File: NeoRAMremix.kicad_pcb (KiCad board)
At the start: 2 copper layers, 58.4 x 88.4 mm, 26 parts, among them P1 C64-Exp-Port, Q1 2N3904, U1 HM628512BFP-5, U2 HM628512BFP-5, U3 HM628512BFP-5, U4 HM628512BFP-5

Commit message: More layout.
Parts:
- moved SJ1 167.2 mm to (90.2, 73.5)
- moved SJ2 153.9 mm to (92.7, 73.5)
- moved SJ3 152.5 mm to (96.5, 73.5)
- moved SJ4 149.4 mm to (99.1, 73.5)
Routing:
- net GND: track 443.4 -> 537.4 mm, vias 7 -> 10
- net +BATT: track 0.00 -> 63.3 mm
- net +5V: track 56.8 -> 80.1 mm, vias 1 -> 4
- net Net-(BT1-Pad1): track 0.00 -> 11.6 mm
- net Net-(SJ3-Pad1): track 0.00 -> 11.2 mm, vias 0 -> 1
- net Net-(SJ4-Pad1): track 0.00 -> 7.01 mm
- net /A7: track 13.3 -> 14.6 mm
- net /A6: track 12.5 -> 13.7 mm

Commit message: More layout.
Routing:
- net /RA15: track 0.00 -> 88.8 mm, vias 0 -> 1
- net Net-(U4-Pad24): track 0.00 -> 85.9 mm, vias 0 -> 1
- net /RA13: track 0.00 -> 79.7 mm, vias 0 -> 1
- net Net-(U4-Pad29): track 0.00 -> 79.7 mm, vias 0 -> 1
- net /RA17: track 0.00 -> 78.1 mm, vias 0 -> 1
- net /RA18: track 0.00 -> 74.8 mm, vias 0 -> 1
- net /RA8: track 0.00 -> 73.6 mm, vias 0 -> 1
- net /RA9: track 0.00 -> 72.4 mm, vias 0 -> 1
- net /RA16: track 0.00 -> 68.3 mm, vias 0 -> 1
- net /RA12: track 0.00 -> 66.7 mm, vias 0 -> 1
- net /RA11: track 0.00 -> 65.2 mm, vias 0 -> 1
- net /RA14: track 0.00 -> 64.7 mm, vias 0 -> 1
- net Net-(U3-Pad24): track 0.00 -> 59.3 mm, vias 0 -> 1
- net /D3: track 69.9 -> 126.7 mm, vias 0 -> 1
- net /D4: track 71.5 -> 123.8 mm, vias 0 -> 2
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
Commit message: First complete layout.
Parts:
- added G***: LOGO, Logo:bigby2, F.Cu at (113.2, 59.3)
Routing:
- net /A6: track 61.0 -> 132.0 mm, vias 1 -> 4
- net /A7: track 61.9 -> 120.7 mm, vias 1 -> 3
- net Net-(V1-Pad7): track 0.00 -> 45.5 mm
- net /A0: track 60.6 -> 102.2 mm, vias 1 -> 2
- net Net-(Q1-Pad3): track 51.3 -> 91.7 mm, vias 0 -> 1
- net Net-(SJ3-Pad1): track 11.2 -> 50.4 mm
- net Net-(SJ4-Pad1): track 7.01 -> 42.6 mm
- net Net-(V1-Pad9): track 0.00 -> 25.1 mm
- net /RA15: track 88.8 -> 68.6 mm
- net GND: track 566.7 -> 577.9 mm
- net /D3: track 126.7 -> 128.9 mm

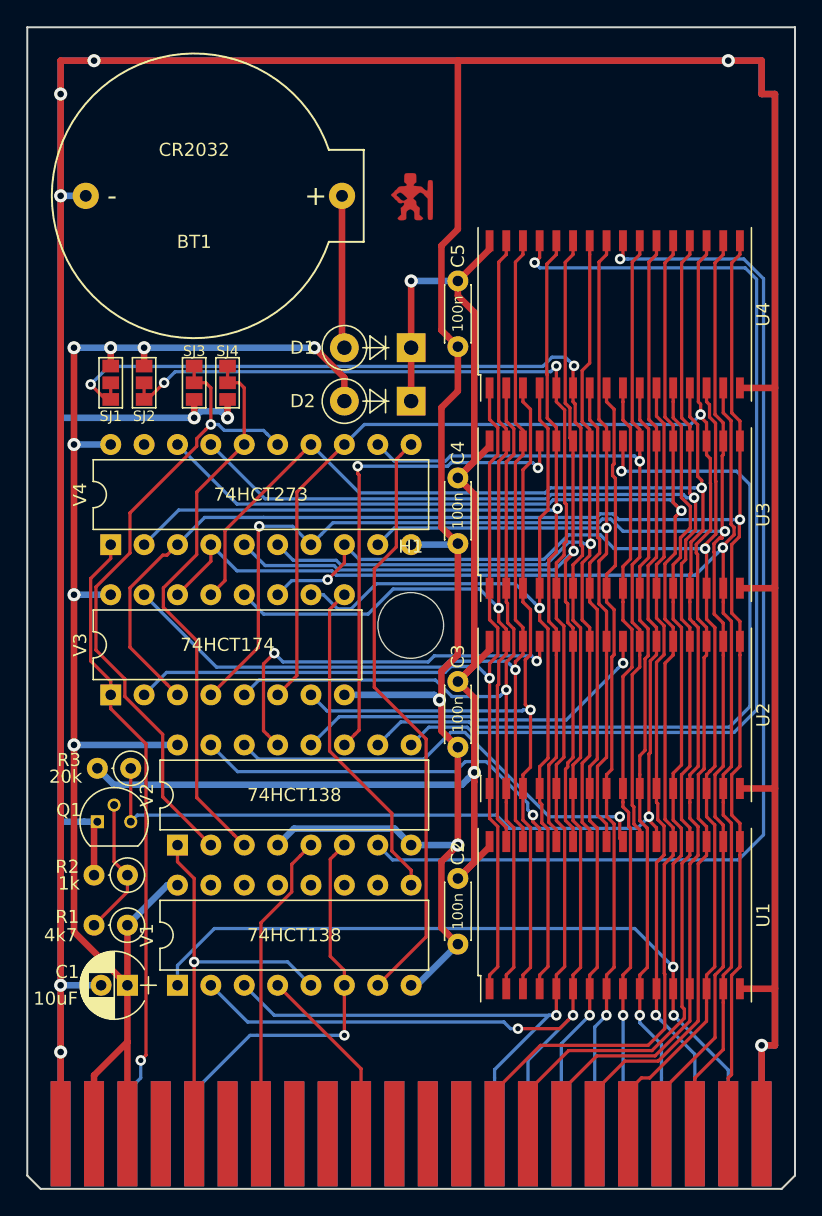
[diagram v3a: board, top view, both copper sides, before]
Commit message: Reset switch.
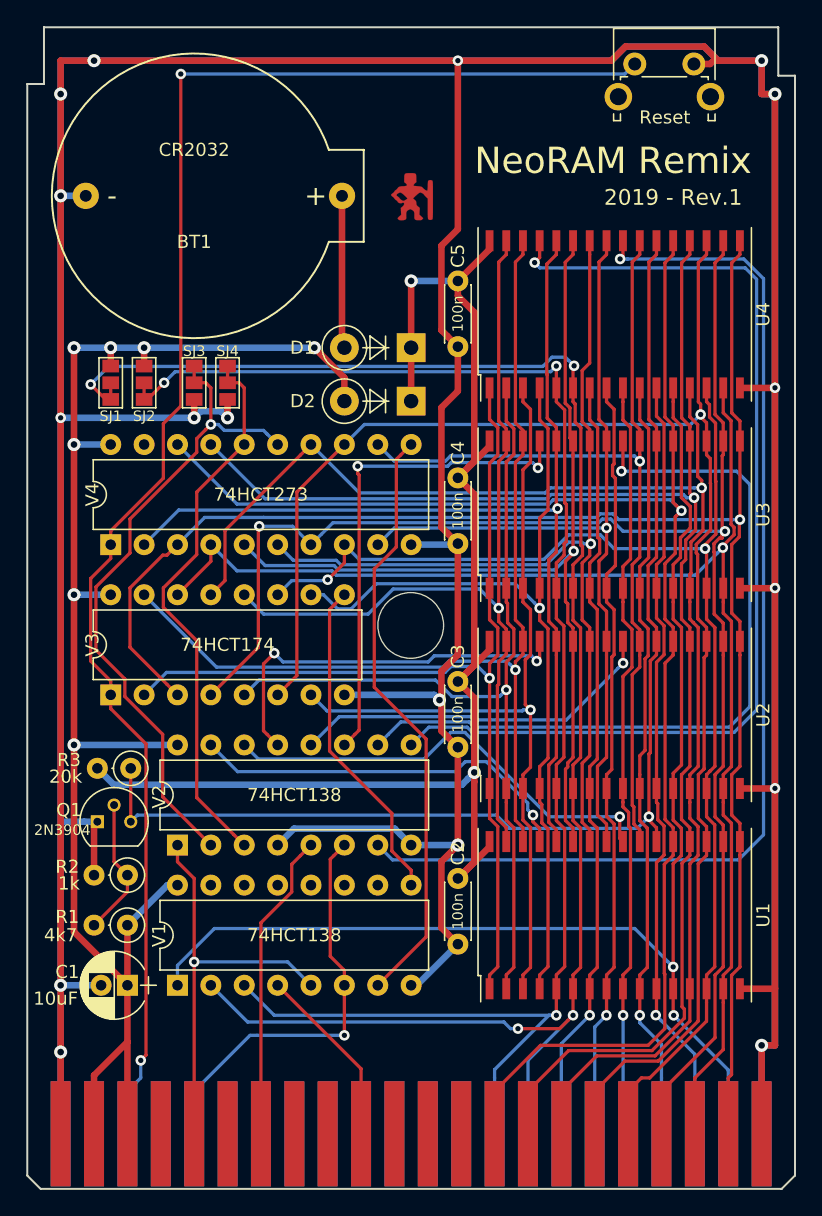
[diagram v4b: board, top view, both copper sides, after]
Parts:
- added SW1: Reset, Buttons_Switches_THT:SW_Tactile_SPST_Angled_PTS645Vx83-2LFS, F.Cu at (130.0, 49.3)
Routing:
- net Net-(P1-PadC): track 47.8 -> 120.7 mm, vias 1 -> 2
- net GND: track 577.9 -> 582.0 mm, vias 11 -> 17
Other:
- outline, holes or cut-outs redrawn
- board text added: "2019 - Rev.1"
- board text added: "NeoRAM Remix"

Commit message: Reduced board size and updated layout.
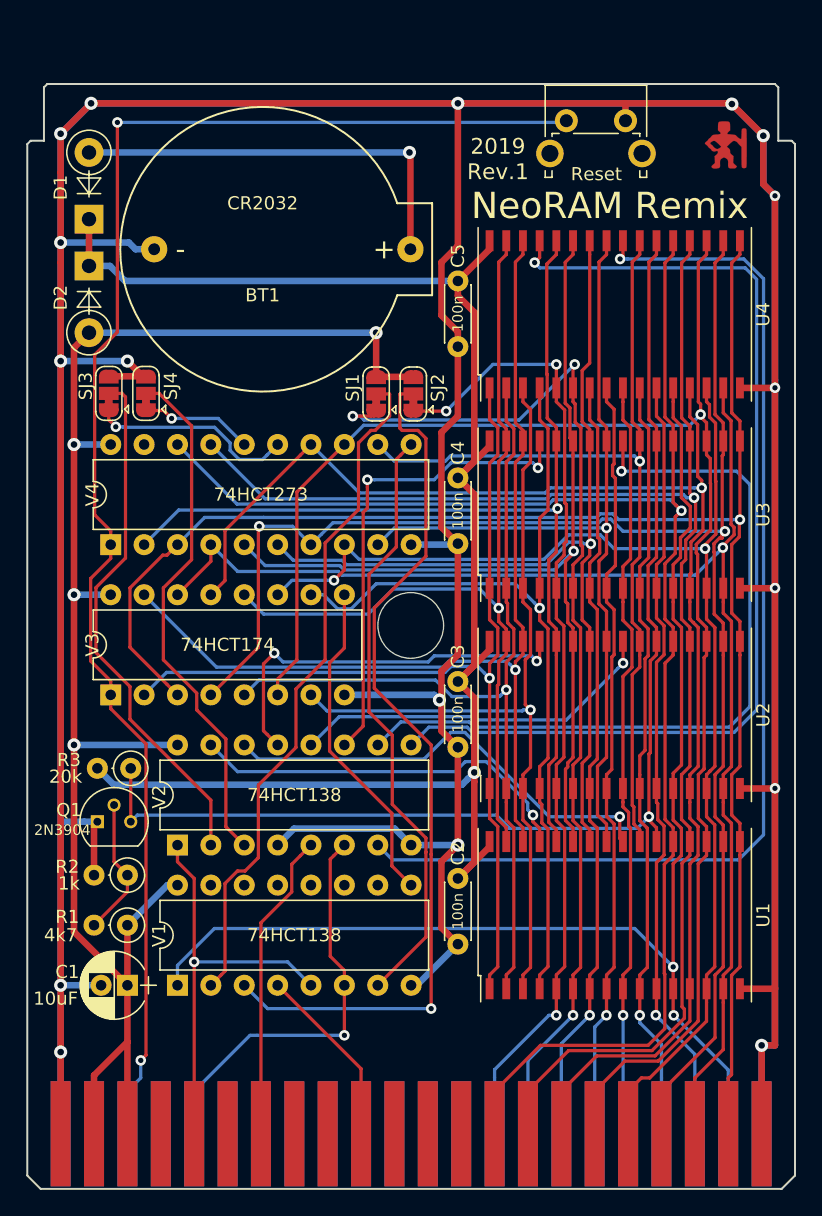
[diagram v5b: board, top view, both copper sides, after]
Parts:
- SJ1, SJ2, SJ3, SJ4: value GS3 -> (none); footprint Connectors:GS3 -> Jumper:SolderJumper-3_P1.3mm_Bridged12_RoundedPad1.0x1.5mm
- moved D2 26.6 mm to (88.5, 64.6), turned to 270 degrees
- moved D1 26.4 mm to (88.5, 61.1), turned to 90 degrees
- moved G*** 24.2 mm to (137.0, 55.4)
- moved SJ2 20.5 mm to (113.2, 74.4), turned to 90 degrees
- moved SJ1 20.2 mm to (110.4, 74.4), turned to 90 degrees
- moved SW1 6.76 mm to (124.8, 53.6)
- moved BT1 6.61 mm to (101.7, 63.4)
- moved SJ3 6.55 mm to (90.0, 74.3), turned to 90 degrees
- moved SJ4 6.26 mm to (92.9, 74.3), turned to 90 degrees
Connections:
- SJ1 pad 1: +5V -> /A6
- SJ1 pad 2: /A6 -> Net-(SJ1-Pad2)
- SJ1 pad 3: /A6 -> +5V
- SJ2 pad 1: +5V -> /A7
- SJ2 pad 2: /A7 -> Net-(SJ2-Pad2)
- SJ2 pad 3: /A7 -> +5V
- SJ3 pad 2: Net-(SJ3-Pad1) -> Net-(SJ3-Pad2)
- SJ4 pad 2: Net-(SJ4-Pad1) -> Net-(SJ4-Pad2)
- V1 pad 2: /A6 -> Net-(SJ1-Pad2)
- V1 pad 3: /A7 -> Net-(SJ2-Pad2)
- V2 pad 2: Net-(SJ3-Pad1) -> Net-(SJ3-Pad2)
- V2 pad 3: Net-(SJ4-Pad1) -> Net-(SJ4-Pad2)
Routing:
- net Net-(SJ2-Pad2): track 0.00 -> 67.7 mm, vias 0 -> 1
- net Net-(SJ1-Pad2): track 0.00 -> 52.2 mm
- net /A6: track 132.0 -> 82.3 mm, vias 4 -> 3
- net /A7: track 120.7 -> 74.8 mm
- net Net-(SJ3-Pad2): track 0.00 -> 40.0 mm
- net Net-(SJ4-Pad2): track 0.00 -> 39.8 mm
- net Net-(SJ3-Pad1): track 50.4 -> 15.6 mm
- net Net-(SJ4-Pad1): track 42.6 -> 8.55 mm, vias 0 -> 1
- net GND: track 582.0 -> 555.7 mm
- net Net-(BT1-Pad1): track 11.6 -> 31.8 mm, vias 0 -> 1
- net +BATT: track 106.6 -> 126.0 mm, vias 2 -> 1
- net Net-(P1-PadC): track 120.7 -> 115.4 mm
- net +5V: track 118.7 -> 122.3 mm, vias 7 -> 4
- net Net-(U3-Pad29): track 37.8 -> 36.7 mm
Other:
- board size 58.4 x 88.4 mm -> 58.4 x 84.1 mm
- board text added: "2019 Rev.1"
- board text removed: "2019 - Rev.1"

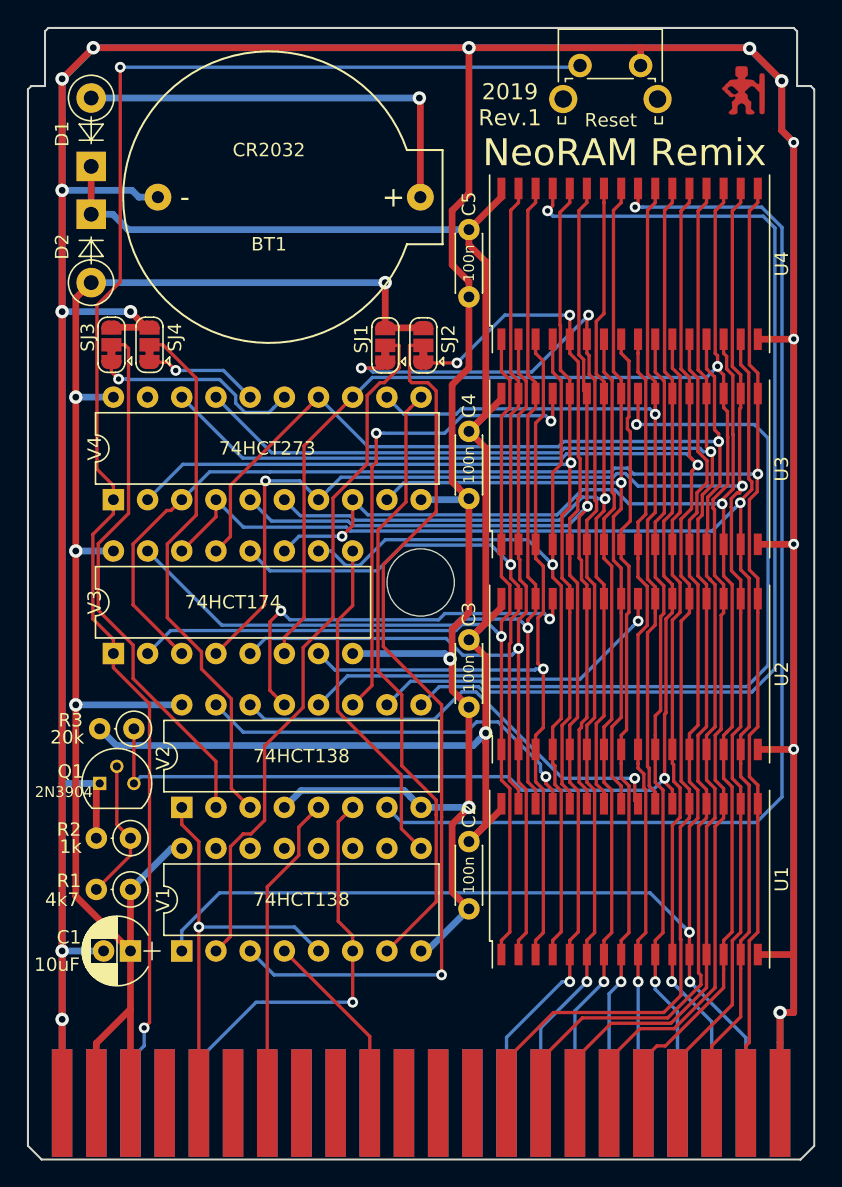
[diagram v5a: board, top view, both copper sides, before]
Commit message: Reduced board width.
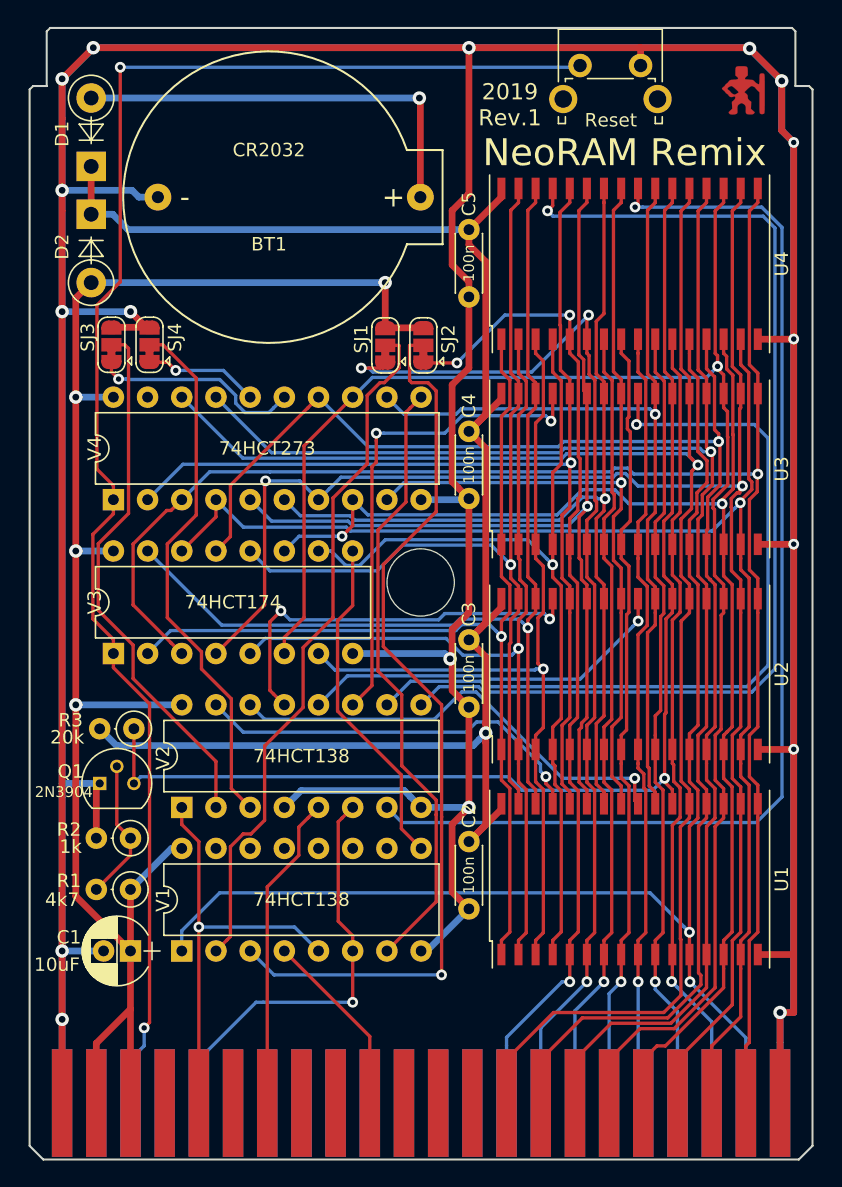
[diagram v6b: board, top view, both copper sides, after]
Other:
- board size 58.4 x 84.1 mm -> 58.2 x 84.1 mm
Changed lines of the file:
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@@
     (41 Cmts.User user)
     (42 Eco1.User user hide)
-    (43 Eco2.User user hide)
+    (43 Eco2.User user)
     (44 Edge.Cuts user)
     (45 Margin user)
@@
     (pad_to_mask_clearance 0.051)
     (solder_mask_min_width 0.25)
-    (aux_axis_origin 83.82 134.874)
+    (aux_axis_origin 83.947 134.874)
     (visible_elements 7FFFFFFF)
     (pcbplotparams
@@
       (net 78 "Net-(SJ4-Pad2)"))
   )
-  (gr_line (start 142.24 55.372) (end 141.986 55.118) (layer Edge.Cuts) (width 0.15))
-  (gr_line (start 140.716 50.8) (end 140.97 51.054) (layer Edge.Cuts) (width 0.15))
-  (gr_line (start 85.09 51.054) (end 85.344 50.8) (layer Edge.Cuts) (width 0.15))
-  (gr_line (start 83.82 55.372) (end 84.074 55.118) (layer Edge.Cuts) (width 0.15))
+  (gr_line (start 142.113 55.372) (end 141.859 55.118) (layer Edge.Cuts) (width 0.15))
+  (gr_line (start 140.589 50.8) (end 140.843 51.054) (layer Edge.Cuts) (width 0.15))
+  (gr_line (start 85.217 51.054) (end 85.471 50.8) (layer Edge.Cuts) (width 0.15))
+  (gr_line (start 83.947 55.372) (end 84.201 55.118) (layer Edge.Cuts) (width 0.15))
   (gr_line (start 83.82 50.8) (end 142.24 50.8) (layer Eco1.User) (width 0.2))
   (gr_text "2019\nRev.1" (at 119.634 56.515) (layer F.SilkS)
@@
     (effects (font (size 2 2) (thickness 0.45)))
   )
-  (gr_line (start 85.09 55.118) (end 84.074 55.118) (layer Edge.Cuts) (width 0.15))
-  (gr_line (start 85.09 51.054) (end 85.09 55.118) (layer Edge.Cuts) (width 0.15))
-  (gr_line (start 140.97 55.118) (end 141.986 55.118) (layer Edge.Cuts) (width 0.15))
-  (gr_line (start 140.97 51.054) (end 140.97 55.118) (layer Edge.Cuts) (width 0.15))
-  (gr_line (start 85.344 50.8) (end 140.716 50.8) (layer Edge.Cuts) (width 0.15))
-  (gr_line (start 83.82 55.372) (end 83.82 133.858) (layer Edge.Cuts) (width 0.15))
-  (gr_line (start 142.24 133.858) (end 142.24 55.372) (layer Edge.Cuts) (width 0.15))
-  (gr_line (start 141.224 134.874) (end 142.24 133.858) (layer Edge.Cuts) (width 0.15))
-  (gr_line (start 84.836 134.874) (end 141.224 134.874) (layer Edge.Cuts) (width 0.15))
-  (gr_line (start 83.82 133.858) (end 84.836 134.874) (layer Edge.Cuts) (width 0.15))
+  (gr_line (start 85.217 55.118) (end 84.201 55.118) (layer Edge.Cuts) (width 0.15))
+  (gr_line (start 85.217 51.054) (end 85.217 55.118) (layer Edge.Cuts) (width 0.15))
+  (gr_line (start 140.843 55.118) (end 141.859 55.118) (layer Edge.Cuts) (width 0.15))
+  (gr_line (start 140.843 51.054) (end 140.843 55.118) (layer Edge.Cuts) (width 0.15))
+  (gr_line (start 85.471 50.8) (end 140.589 50.8) (layer Edge.Cuts) (width 0.15))
+  (gr_line (start 83.947 55.372) (end 83.947 133.858) (layer Edge.Cuts) (width 0.15))
+  (gr_line (start 142.113 133.858) (end 142.113 55.372) (layer Edge.Cuts) (width 0.15))
+  (gr_line (start 141.097 134.874) (end 142.113 133.858) (layer Edge.Cuts) (width 0.15))
+  (gr_line (start 84.963 134.874) (end 141.097 134.874) (layer Edge.Cuts) (width 0.15))
+  (gr_line (start 83.947 133.858) (end 84.963 134.874) (layer Edge.Cuts) (width 0.15))
   (gr_line (start 142.24 134.874) (end 83.82 134.874) (layer Eco1.User) (width 0.2))
   (gr_line (start 142.24 50.8) (end 142.24 134.874) (layer Eco1.User) (width 0.2))
